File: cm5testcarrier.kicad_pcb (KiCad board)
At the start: 2 copper layers, 100 x 100 mm, 41 parts, among them J2_servos8-15 2091-1372, J3_5v1 2091-1372, J4_servos0-7 2091-1372, U4 PCA9685

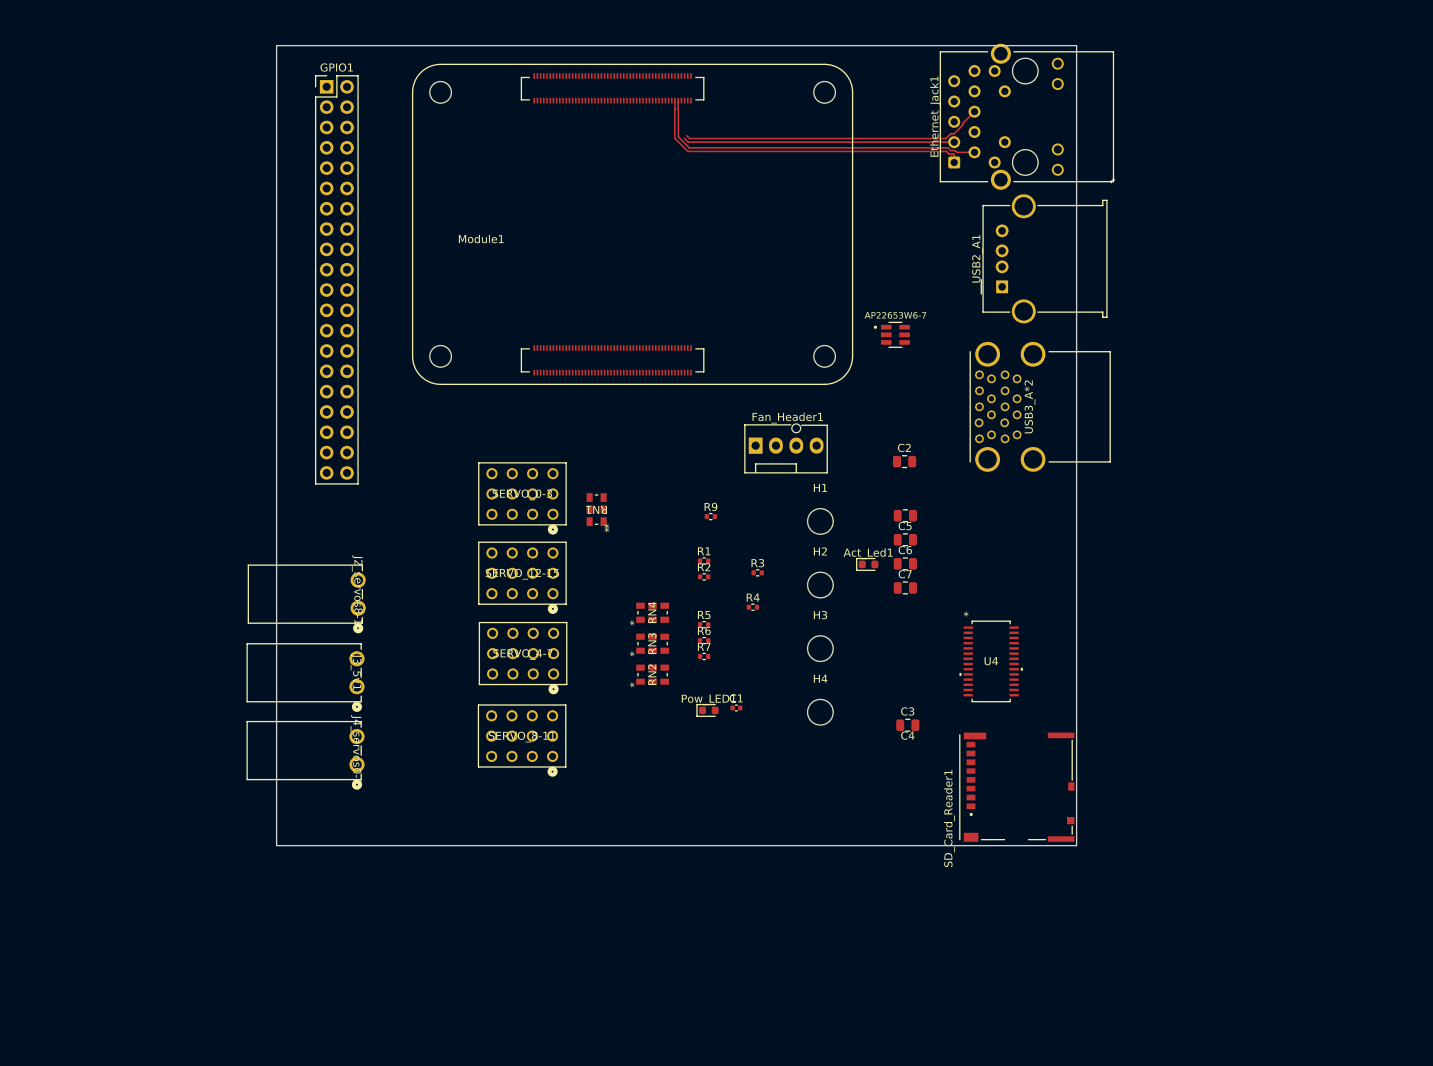
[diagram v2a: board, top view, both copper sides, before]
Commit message: Add CSI connector footprint, symbol, and model
 - Partially routed USB 3.0
 - routed ethernet
 - added LEDs
 - updated BOM
 - switched passives to 0805 to save space
 - added CSI/DSI ports (still unrouted)
 - adjusted placement of ports
 - updated README w/ more detailed descriptions
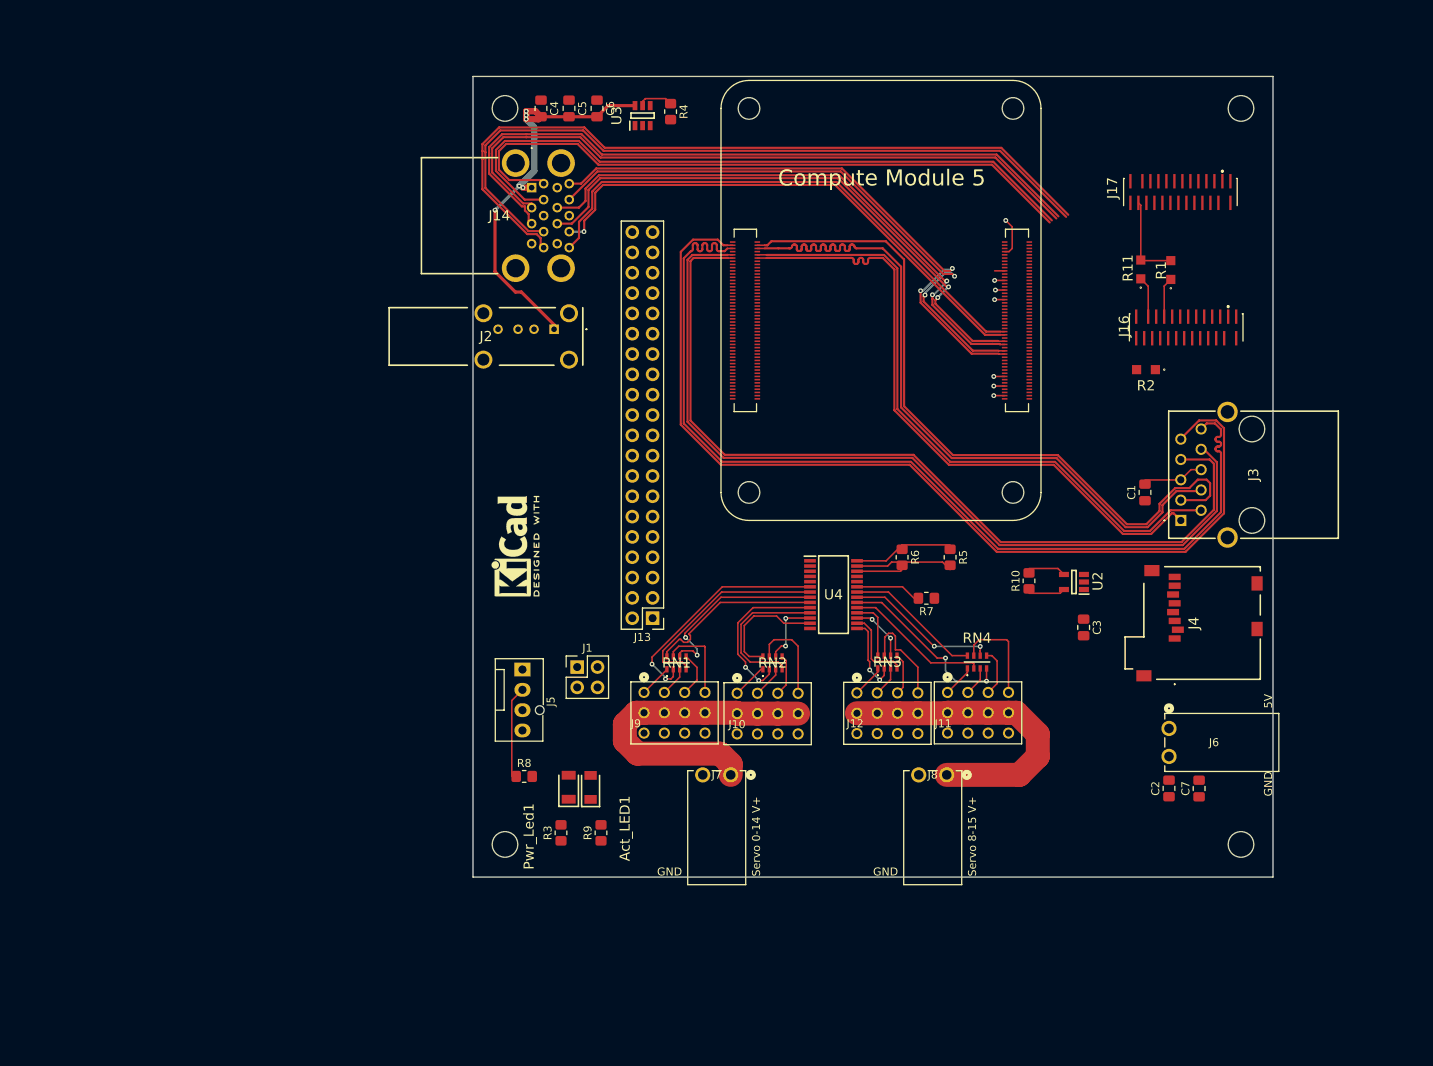
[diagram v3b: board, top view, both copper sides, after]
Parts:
- removed AP22653W6-7: U3, RoboSubCompute.footprints:USB_Current_limit_Switch_AP22653W6-7
- removed Act_Led1: D2, LED_SMD:LED_0603_1608Metric
- removed Ethernet_Jack1: MagJack-A70-112-331N126, RoboSubCompute.footprints:ethernet_jack
- removed Fan_Header1: Conn_01x04_Pin, Connector:FanPinHeader_1x04_P2.54mm_Vertical
- removed GPIO1: Conn_02x20_Odd_Even, Connector_PinHeader_2.54mm:PinHeader_2x20_P2.54mm_Vertical
- removed J2_servos8-15, J3_5v1, J4_servos0-7: 2091-1372, RoboSubCompute.footprints:CONN2_2091-1372_WAGO
- removed Pow_LED1: D1, LED_SMD:LED_0603_1608Metric
- removed SD_Card_Reader1: Micro_SD_Card_Det2, RoboSubCompute.footprints:SDCARD_MOLEX_503398-1892
- removed SERVO_0-3, SERVO_12-15, SERVO_4-7, SERVO_8-11: HEADER-3X04, RoboSubCompute.footprints:CON12_3X4_TU_TSW_SAI
- removed USB2_A1: J2, Connector_USB:USB_A_Molex_67643_Horizontal
- removed USB3_A*2: J3, RoboSubCompute.footprints:USB3.0_2x_conn
- added Act_LED1: 150120GS75000, SamacSys_Parts:LEDC3214X68N, F.Cu at (128.8, 132.2)
- added J1: Disable Bluetooth/Wifi, Connector_PinHeader_2.54mm:PinHeader_2x02_P2.54mm_Vertical, F.Cu at (127.1, 117.2)
- added J10: HEADER-3X04, RoboSubCompute.footprints:CON12_3X4_TU_TSW_SAI, F.Cu at (150.9, 123.0)
- added J11: HEADER-3X04, RoboSubCompute.footprints:CON12_3X4_TU_TSW_SAI, F.Cu at (177.2, 122.9)
- added J12: HEADER-3X04, RoboSubCompute.footprints:CON12_3X4_TU_TSW_SAI, F.Cu at (165.8, 123.0)
- added J13: Conn_02x20_Odd_Even, Connector_PinHeader_2.54mm:PinHeader_2x20_P2.54mm_Vertical, F.Cu at (136.5, 111.1)
- added J14: GSB3112311HR, SamacSys_Parts:GSB3112311HR, F.Cu at (121.4, 57.2)
- added J16: TF38-22S-0.5SV_830_, SamacSys_Parts:TF3822S05SV830, F.Cu at (203.2, 73.0)
- added J17: TF38-22S-0.5SV_830_, SamacSys_Parts:TF3822S05SV830, F.Cu at (202.5, 56.1)
- added J2: GSB191217FHR, SamacSys_Parts:GSB191217FHR, F.Cu at (124.2, 75.0)
- added J3: ARJM11B1-502-NN-EW2, SamacSys_Parts:ARJM11B1502NNEW2, F.Cu at (202.5, 98.9)
- added J4: GTFP08432B1HR, SamacSys_Parts:GTFP08432B1HR, F.Cu at (204.0, 111.7)
- added J5: Fan_Header, Connector:FanPinHeader_1x04_P2.54mm_Vertical, F.Cu at (120.2, 117.5)
- added J6: Wago connector 2091-1372, RoboSubCompute.footprints:CONN2_2091-1372_WAGO, F.Cu at (201.1, 124.8)
- added J7: Wago connector 2091-1372, RoboSubCompute.footprints:CONN2_2091-1372_WAGO, F.Cu at (146.3, 130.7)
- added J8: Wago connector 2091-1372, RoboSubCompute.footprints:CONN2_2091-1372_WAGO, F.Cu at (173.3, 130.7)
- added J9: HEADER-3X04, RoboSubCompute.footprints:CON12_3X4_TU_TSW_SAI, F.Cu at (139.2, 122.9)
- added Pwr_Led1: 150120RS75000, SamacSys_Parts:LEDC3216X68N, F.Cu at (126.0, 132.2)
- added R10: 10K, Resistor_SMD:R_0805_2012Metric_Pad1.20x1.40mm_HandSolder, F.Cu at (183.6, 106.4)
- added R11: 2.2K, SamacSys_Parts:ERJS06_U06__0805_, F.Cu at (197.5, 67.5)
- added R8: 10K, Resistor_SMD:R_0805_2012Metric_Pad1.20x1.40mm_HandSolder, F.Cu at (120.5, 130.8)
- added REF**: KiCad-Logo2_5mm_SilkScreen, Symbol:KiCad-Logo2_5mm_SilkScreen, F.Cu at (119.3, 102.1)
- added U2: RT9742GGJ5, SamacSys_Parts:SOT94P280X100-5N, F.Cu at (189.2, 106.5)
- added U3: AP22653W6-7, SamacSys_Parts:SOT95P280X145-6N, F.Cu at (135.2, 48.2)
- C1: value 100n -> 100p; footprint Capacitor_SMD:C_0402_1005Metric -> Capacitor_SMD:C_0805_2012Metric_Pad1.18x1.45mm_HandSolder
- C2, C3, C5, C6: footprint Capacitor_SMD:C_0805_2012Metric -> Capacitor_SMD:C_0805_2012Metric_Pad1.18x1.45mm_HandSolder
- C4: value 100uF -> 100u; footprint Capacitor_SMD:C_0805_2012Metric -> Capacitor_SMD:C_0805_2012Metric_Pad1.18x1.45mm_HandSolder
- C7: value 10uF -> 10u; footprint Capacitor_SMD:C_0805_2012Metric -> Capacitor_SMD:C_0805_2012Metric_Pad1.18x1.45mm_HandSolder
- R1, R2: value 470R -> 2.2K; footprint Resistor_SMD:R_0402_1005Metric -> SamacSys_Parts:ERJS06_U06__0805_
- R3: value 1k -> 150; footprint Resistor_SMD:R_0402_1005Metric -> Resistor_SMD:R_0805_2012Metric_Pad1.20x1.40mm_HandSolder
- R4: value 10k 1% -> 10k; footprint Resistor_SMD:R_0402_1005Metric -> Resistor_SMD:R_0805_2012Metric_Pad1.20x1.40mm_HandSolder
- R5, R6, R7: footprint Resistor_SMD:R_0402_1005Metric -> Resistor_SMD:R_0805_2012Metric_Pad1.20x1.40mm_HandSolder
- R9: value 1k -> 90; footprint Resistor_SMD:R_0402_1005Metric -> Resistor_SMD:R_0805_2012Metric_Pad1.20x1.40mm_HandSolder
- RN1, RN2, RN3, RN4: footprint RoboSubCompute.footprints:4x_220_resistor_net -> SamacSys_Parts:CAT161000F4
- U4: value PCA9685 -> PCA9685PW,118; footprint RoboSubCompute.footprints:servo_controller_pca9685 -> SamacSys_Parts:SOP65P640X110-28N
- moved H4 92.0 mm to (210.1, 47.4)
- moved H2 71.4 mm to (118.0, 47.4)
- moved C6 68.7 mm to (129.6, 47.4), turned to -90 degrees
- moved R1 68.7 mm to (201.3, 67.5), turned to 90 degrees
- moved C5 68.4 mm to (126.0, 47.4), turned to -90 degrees
- moved C4 68.3 mm to (122.5, 47.4), turned to -90 degrees
- moved Module1 63.1 mm to (148.6, 95.3), turned to 0 degrees
- moved R4 62.8 mm to (138.8, 47.8), turned to -90 degrees
- moved R2 61.0 mm to (198.2, 80.0), turned to 180 degrees
- moved H3 58.0 mm to (210.1, 139.3), turned to 180 degrees
- moved C1 57.7 mm to (198.1, 95.3), turned to 90 degrees
- moved H1 56.4 mm to (118.0, 139.3)
- moved C2 52.5 mm to (201.1, 132.3), turned to 90 degrees
- moved C7 44.5 mm to (204.8, 132.4), turned to 90 degrees
- moved R9 41.8 mm to (130.1, 137.9), turned to 90 degrees
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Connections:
- Module1 pad 100: unconnected-(Module1A-CAM_GPIO1-Pad100) -> /CAM_GPIO1
- Module1 pad 115: unconnected-(Module1B-MIPI0_D0_N-Pad115) -> /DPHY0_D0_N
- Module1 pad 117: unconnected-(Module1B-MIPI0_D0_P-Pad117) -> /DPHY0_D0_P
- Module1 pad 121: unconnected-(Module1B-MIPI0_D1_N-Pad121) -> /DPHY0_D1_N
- Module1 pad 123: unconnected-(Module1B-MIPI0_D1_P-Pad123) -> /DPHY0_D1_P
- Module1 pad 127: unconnected-(Module1B-MIPI0_C_N-Pad127) -> /DPHY0_C_N
- Module1 pad 128: unconnected-(Module1B-USB3-0-RX_N-Pad128) -> /USB3-0-RX_N
- Module1 pad 129: unconnected-(Module1B-MIPI0_C_P-Pad129) -> /DPHY0_C_P
- Module1 pad 133: unconnected-(Module1B-MIPI0_D2_N-Pad133) -> /DPHY0_D2_N
- Module1 pad 135: unconnected-(Module1B-MIPI0_D2_P-Pad135) -> /DPHY0_D2_P
- Module1 pad 139: unconnected-(Module1B-MIPI0_D3_N-Pad139) -> /DPHY0_D3_N
- Module1 pad 141: unconnected-(Module1B-MIPI0_D3_P-Pad141) -> /DPHY0_D3_P
- Module1 pad 15: /led1 -> unconnected-(Module1A-Ethernet_nLED3(3.3v)-Pad15)
- Module1 pad 17: /led2 -> unconnected-(Module1A-Ethernet_nLED2(3.3v)-Pad17)
- Module1 pad 175: unconnected-(Module1B-MIPI1_D0_N-Pad175) -> /DPHY1_D0_N
- Module1 pad 177: unconnected-(Module1B-MIPI1_D0_P-Pad177) -> /DPHY1_D0_P
- Module1 pad 181: unconnected-(Module1B-MIPI1_D1_N-Pad181) -> /DPHY1_D1_N
- Module1 pad 183: unconnected-(Module1B-MIPI1_D1_P-Pad183) -> /DPHY1_D1_P
- Module1 pad 187: unconnected-(Module1B-MIPI1_C_N-Pad187) -> /DPHY1_C_N
- Module1 pad 189: unconnected-(Module1B-MIPI1_C_P-Pad189) -> /DPHY1_C_P
- Module1 pad 193: unconnected-(Module1B-MIPI1_D2_N-Pad193) -> /DPHY1_D2_N
- Module1 pad 194: unconnected-(Module1B-MIPI1_D3_N-Pad194) -> /DPHY1_D3_N
- Module1 pad 195: unconnected-(Module1B-MIPI1_D2_P-Pad195) -> /DPHY1_D2_P
- Module1 pad 196: unconnected-(Module1B-MIPI1_D3_P-Pad196) -> /DPHY1_D3_P
- Module1 pad 4: /p+2 -> /p+1
- Module1 pad 62: unconnected-(Module1A-SD_CMD-Pad62) -> /SD_CMD
- Module1 pad 80: /PCA_SCL -> /SCL0
- Module1 pad 82: /PCA_SDA -> /SDA0
- Module1 pad 97: unconnected-(Module1A-CAM_GPIO0-Pad97) -> /CAM_GPIO0
- R1 pad 2: /led1 -> +3V3
- R2 pad 1: Net-(Ethernet_Jack1-LEDG_K) -> /GPIO1
- R2 pad 2: /led2 -> +3V3
- R5 pad 2: /PCA_SDA -> /GPIO2
- R6 pad 2: /PCA_SCL -> /GPIO3
- U4 pad 26: /PCA_SCL -> /GPIO3
- U4 pad 27: /PCA_SDA -> /GPIO2
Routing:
- net /p+3: track 0.00 -> 122.9 mm
- net /p-3: track 0.00 -> 122.7 mm
- net /p-2: track 0.00 -> 109.2 mm
- net /p+2: track 0.00 -> 109.0 mm
- net /USB3-0-RX_N: track 0.00 -> 95.4 mm
- net /USB3-0-RX_P: track 0.00 -> 92.7 mm
- net /USB3-0-D_P: track 0.00 -> 88.1 mm
- net /USB3-0-D_N: track 0.00 -> 85.4 mm
- net /USB3-0-TX_N: track 0.00 -> 84.1 mm
- net /USB3-0-TX_P: track 0.00 -> 81.9 mm
- net /USB3-1-TX_P: track 0.00 -> 73.9 mm, vias 0 -> 2
- net /USB3-1-TX_N: track 0.00 -> 73.8 mm, vias 0 -> 2
- net /USB3-1-D_P: track 0.00 -> 71.8 mm, vias 0 -> 2
- net /USB3-1-D_N: track 0.00 -> 71.7 mm, vias 0 -> 2
- net /USB3-1-RX_N: track 0.00 -> 68.0 mm
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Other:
- board size 100 x 100 mm -> 100 x 100.1 mm
- board text added: "5V"
- board text added: "Compute Module 5"
- board text added: "GND"
- board text added: "Servo 0-14 V+"
- board text added: "Servo 8-15 V+"

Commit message: V1 Done
- finished routing traces
- filled ground planes
- started readme documentation
- resized power traces for power needs
- relocated the servo setup to allow for better placement of the GPIO
- relocated some ports for better diff pair routing
- swapped cm5 board orientation for better routing (also doesn't matter because wireless will be unused)
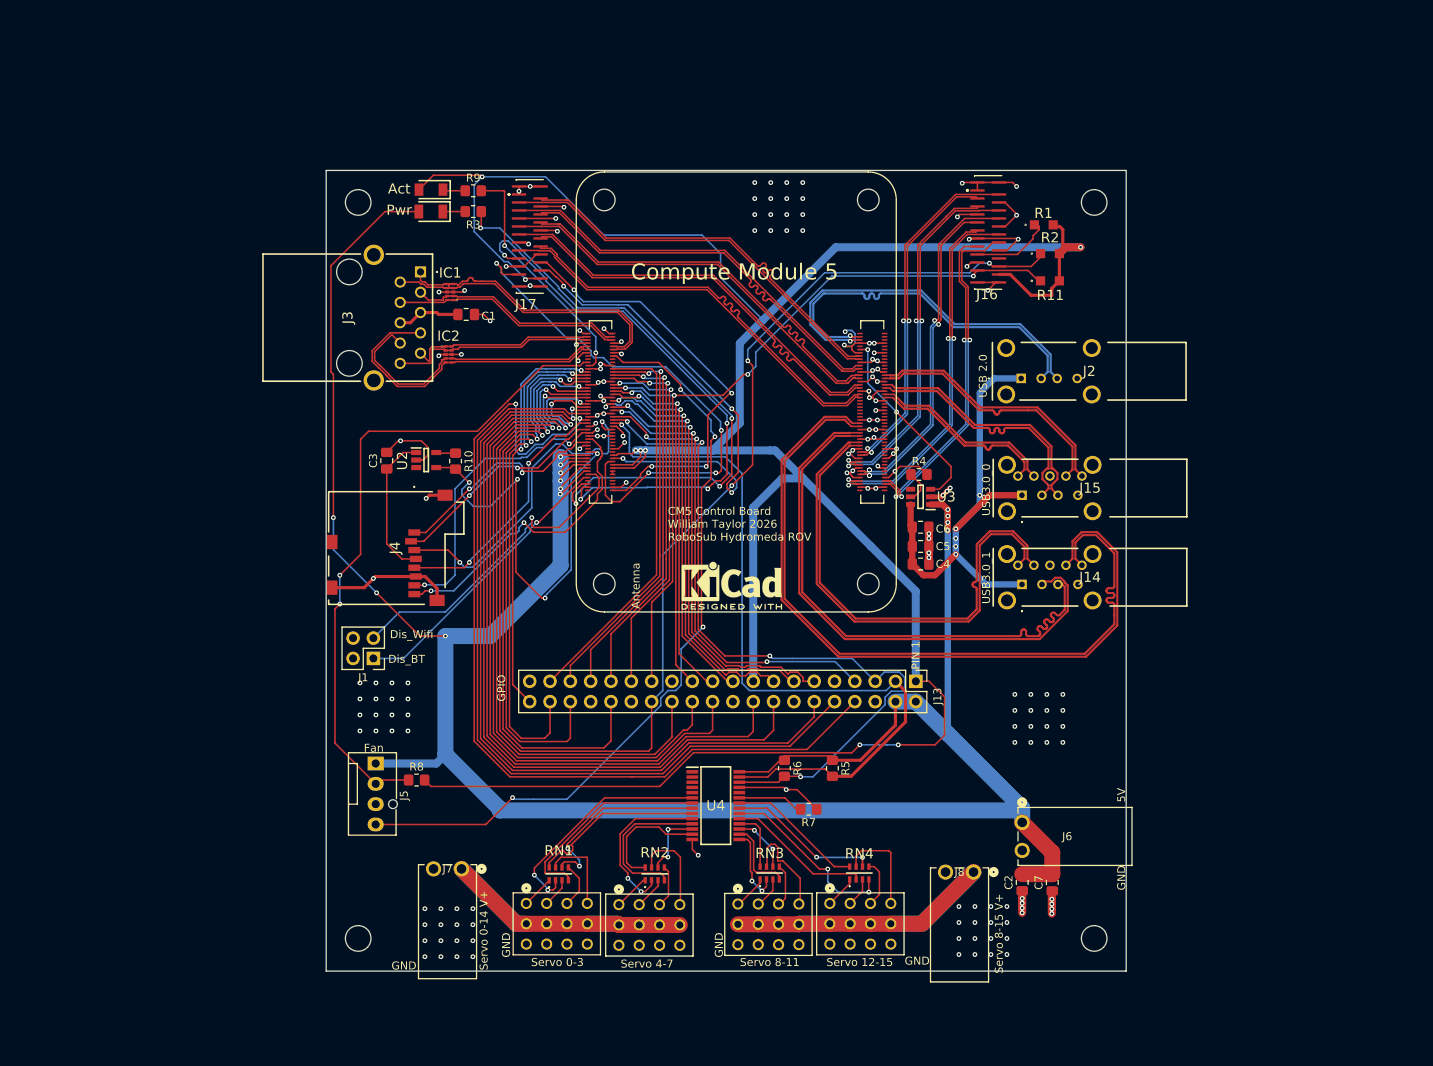
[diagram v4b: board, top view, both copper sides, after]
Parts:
- added IC1: TPD4E05U06QDQARQ1, SamacSys_Parts:DQA_R-PUSON-N10_, F.Cu at (111.2, 70.3)
- added IC2: TPD4E05U06QDQARQ1, SamacSys_Parts:DQA_R-PUSON-N10_, F.Cu at (111.0, 78.1)
- added J15: GSB3116344KHHR, SamacSys_Parts:GSB3116344KHHR, F.Cu at (182.7, 95.7)
- J14: value GSB3112311HR -> GSB3116344KHHR; footprint SamacSys_Parts:GSB3112311HR -> SamacSys_Parts:GSB3116344KHHR
- moved J4 100.0 mm to (104.5, 102.3), turned to 90 degrees
- moved J3 100.0 mm to (107.5, 67.8), turned to -90 degrees
- moved C3 89.6 mm to (103.3, 91.4), turned to 90 degrees
- moved C1 87.7 mm to (113.2, 73.1), turned to 180 degrees
- moved J17 83.3 mm to (119.5, 63.4), turned to 90 degrees
- moved U2 82.4 mm to (108.2, 91.3), turned to 0 degrees
- moved R9 81.8 mm to (114.1, 57.6), turned to 180 degrees
- moved J14 78.8 mm to (182.7, 106.8), turned to 180 degrees
- moved R3 78.4 mm to (114.1, 60.2), turned to 180 degrees
- moved Act 77.3 mm to (108.8, 57.5), turned to 180 degrees
- moved C4 74.1 mm to (170.0, 104.3), turned to 180 degrees
- moved Pwr 74.0 mm to (108.8, 60.2), turned to 180 degrees
- moved R10 73.2 mm to (111.9, 91.4), turned to -90 degrees
- moved C5 70.2 mm to (170.0, 102.1), turned to 180 degrees
- moved C6 66.2 mm to (170.0, 99.7), turned to 180 degrees
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- renumbered Act_LED1 to Act, Pwr_Led1 to Pwr
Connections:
- J14 pad 2: /USB3-0-D_N -> /USB3-1-D_P
- J14 pad 3: /USB3-0-D_P -> /USB3-1-D_N
- J14 pad 5: /USB3-0-RX_N -> /USB3-1-RX_P
- J14 pad 6: /USB3-0-RX_P -> /USB3-1-RX_N
- J14 pad 8: /USB3-0-TX_N -> /USB3-1-TX_P
- J14 pad 9: /USB3-0-TX_P -> /USB3-1-TX_N
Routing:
- net +3V3: track 11.1 -> 328.1 mm, vias 0 -> 8
- net +5V: track 12.5 -> 316.8 mm, vias 0 -> 13
- net GND: track 14.1 -> 211.0 mm, vias 7 -> 173
- net /GPIO1: track 0.00 -> 172.9 mm, vias 0 -> 5
- net /GPIO14: track 0.00 -> 115.6 mm, vias 0 -> 2
- net /GPIO15: track 0.00 -> 103.2 mm
- net /GPIO23: track 0.00 -> 102.1 mm, vias 0 -> 2
- net /GPIO18: track 0.00 -> 101.9 mm, vias 0 -> 2
- net /p+3: track 122.9 -> 23.6 mm
- net /GPIO24: track 0.00 -> 98.7 mm, vias 0 -> 2
- net /FAN_TACHOMETER: track 0.00 -> 97.7 mm, vias 0 -> 4
- net /p-3: track 122.7 -> 25.8 mm
- net /GPIO2: track 0.00 -> 96.5 mm, vias 0 -> 1
- net /GPIO0: track 5.11 -> 99.0 mm, vias 0 -> 4
- net /GPIO3: track 0.00 -> 93.1 mm, vias 0 -> 4
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- added copper zone on In1.Cu, net GND
- added copper zone on In2.Cu, net GND
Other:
- copper layers 2 -> 4
- board text added: "Antenna"
- board text added: "CM5 Control Board William Taylor 2026 RoboSub Hydromeda ROV"
- board text added: "Dis_BT"
- board text added: "Dis_Wifi"
- board text added: "Fan"
- board text added: "GPIO"
- board text added: "PIN 1"
- board text added: "Servo 0-3"
- board text added: "Servo 12-15"
- board text added: "Servo 4-7"
- board text added: "Servo 8-11"
- board text added: "USB 2.0"
- board text added: "USB3.0_0"
- board text added: "USB3.0_1"
